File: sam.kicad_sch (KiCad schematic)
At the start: 29 parts, among them IC2 74ACT244N, IC3 74ACT244N, IC4 74ACT02, IC5 74ACT138, IC6 74ACT138N, J1 JTAG, U3 XC95144XL-TQ100, U4 AS6C1008-55TIN, U5 AS6C1008-TIN, X1 14.31818MHz

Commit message: Progress routing
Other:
- moved on the sheet: C5, C6, U5

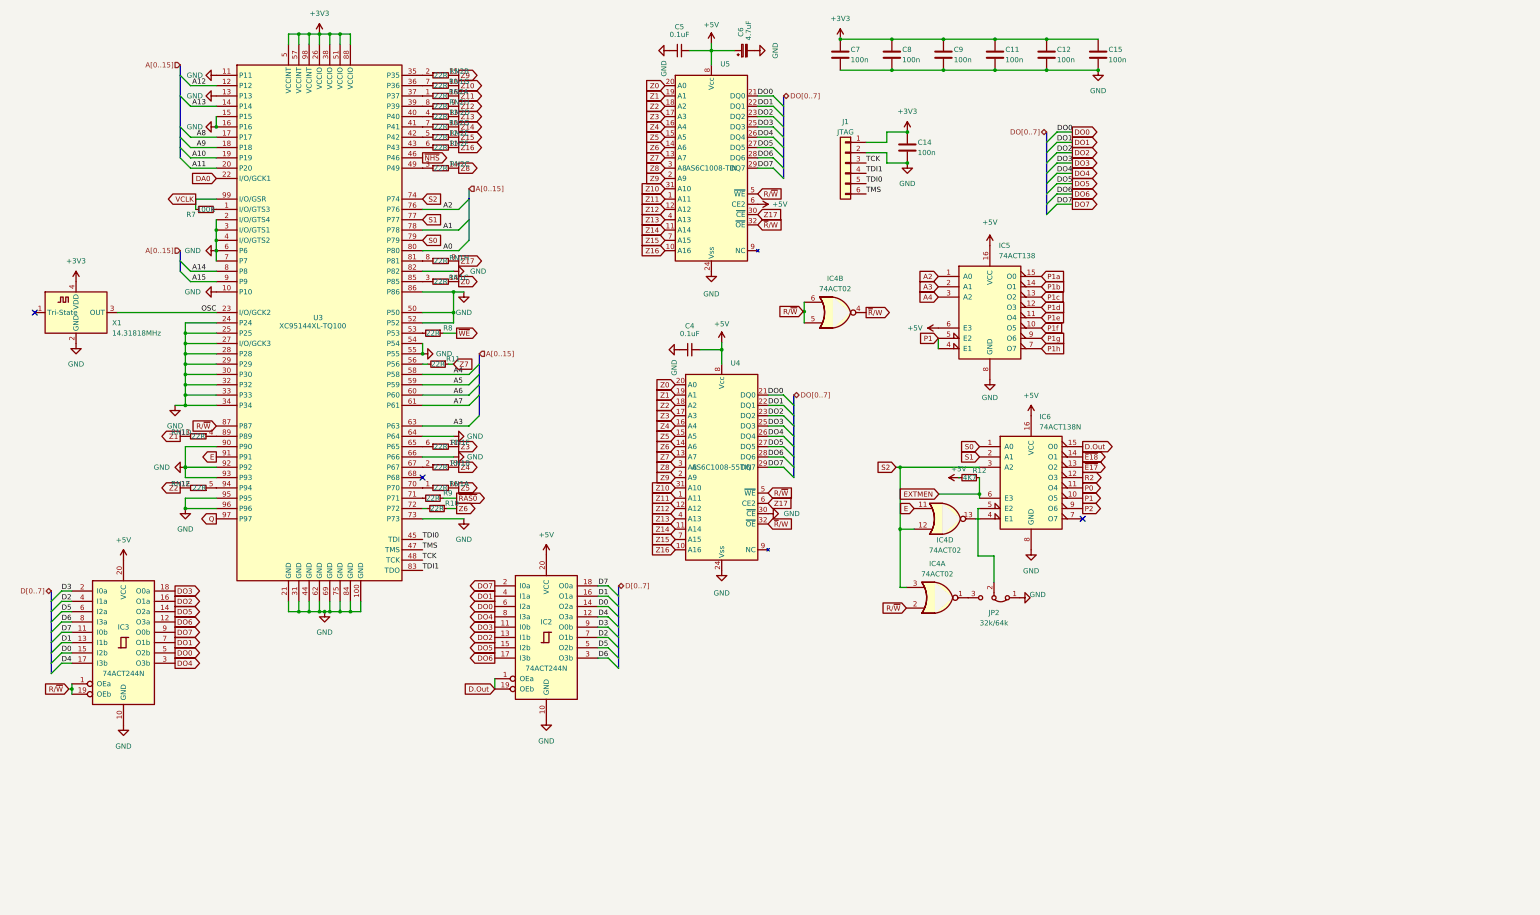
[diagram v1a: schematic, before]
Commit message: rework sram
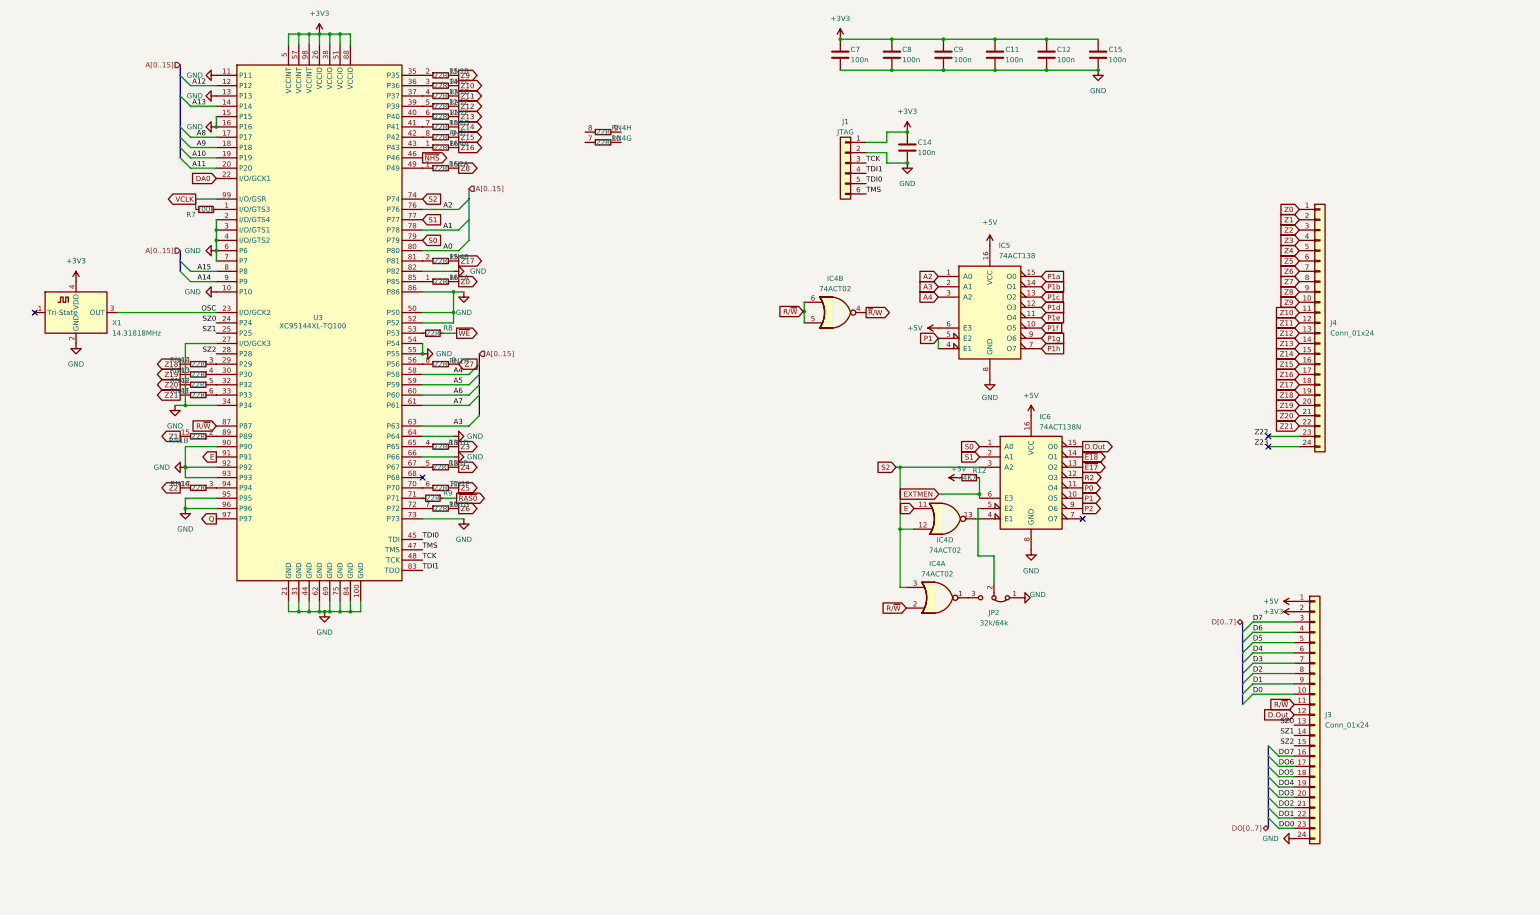
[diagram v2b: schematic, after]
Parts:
- removed C4, C5: 0.1uF, Capacitor_SMD:C_0805_2012Metric_Pad1.18x1.45mm_HandSolder, symbol Device:C_Small
- removed C6: 4.7uF, Capacitor_Tantalum_SMD:CP_EIA-3216-18_Kemet-A_Pad1.58x1.35mm_HandSolder, symbol Device:C_Polarized_Small
- removed IC2, IC3: 74ACT244N, Package_SO:SOIC-20W_7.5x12.8mm_P1.27mm, symbol 74xx:74LS244
- removed R10, R11: 22R, Resistor_SMD:R_0805_2012Metric_Pad1.20x1.40mm_HandSolder, symbol Device:R_Small
- removed U4: AS6C1008-55TIN, Package_SO:TSOP-I-32_18.4x8mm_P0.5mm, symbol Motorola PIA:AS6C1008
- removed U5: AS6C1008-TIN, Package_SO:TSOP-I-32_18.4x8mm_P0.5mm, symbol Motorola PIA:AS6C1008
- added J3, J4: Conn_01x24, Connector_PinSocket_1.27mm:PinSocket_1x24_P1.27mm_Vertical, symbol Connector_Generic:Conn_01x24
- added RN4: 22R, Package_SO:SOIC-16_3.9x9.9mm_P1.27mm, symbol Motorola PIA:R_Pack_Split
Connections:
- net +3V3: now also J3.2 (Pin_2)
- net +5V: now also J3.1 (Pin_1)
- net A14: now also U3.9 (P9); no longer U3.8 (P8)
- net A15: now also U3.8 (P8); no longer U3.9 (P9)
- net D.Out: now also J3.12 (Pin_12)
- net D0: now also J3.10 (Pin_10)
- net D1: now also J3.9 (Pin_9)
- net D2: now also J3.8 (Pin_8)
- net D3: now also J3.7 (Pin_7)
- net D4: now also J3.6 (Pin_6)
- net D5: now also J3.5 (Pin_5)
- net D6: now also J3.4 (Pin_4)
- net D7: now also J3.3 (Pin_3)
- net DO0: now also J3.23 (Pin_23)
- net DO1: now also J3.22 (Pin_22)
- net DO2: now also J3.21 (Pin_21)
- net DO3: now also J3.20 (Pin_20)
- net DO4: now also J3.19 (Pin_19)
- net DO5: now also J3.18 (Pin_18)
- net DO6: now also J3.17 (Pin_17)
- net DO7: now also J3.16 (Pin_16)
- net GND: now also J3.24 (Pin_24); no longer U3.24 (P24), U3.25 (P25), U3.28 (P28), U3.29 (P29), U3.30 (P30), U3.32 (P32), U3.33 (P33)
- net R/~{W}: now also J3.11 (Pin_11)
- net Z0: now also RN1.16, J4.1 (Pin_1); no longer RN1.14
- net Z1: now also RN1.15, J4.2 (Pin_2); no longer RN1.13
- net Z10: now also RN2.14, J4.11 (Pin_11); no longer RN1.10
- net Z11: now also RN2.13, J4.12 (Pin_12); no longer RN2.16
- net Z12: now also RN2.12, J4.13 (Pin_13); no longer RN2.9
- net Z13: now also RN2.11, J4.14 (Pin_14); no longer RN2.13
- net Z14: now also J4.15 (Pin_15)
- net Z15: now also RN2.9, J4.16 (Pin_16); no longer RN2.12
- net Z16: now also J4.17 (Pin_17), RN4.16; no longer RN2.11
- net Z17: now also J4.18 (Pin_18), RN4.15; no longer RN1.9
- net Z2: now also RN1.14, J4.3 (Pin_3); no longer RN1.12
- net Z3: now also RN1.13, J4.4 (Pin_4); no longer RN1.11
- net Z4: now also RN1.12, J4.5 (Pin_5); no longer RN1.15
- net Z5: now also RN1.11, J4.6 (Pin_6); no longer RN1.16
- net Z6: now also RN1.10, J4.7 (Pin_7)
- net Z7: now also RN1.9, J4.8 (Pin_8)
- net Z8: now also RN2.16, J4.9 (Pin_9); no longer RN2.14
- net Z9: now also J4.10 (Pin_10)
- net at RN1.6: now also U3.70 (P70); no longer U3.65 (P65)
- net at RN2.6: now also U3.40 (P40); no longer U3.43 (P43)
- net at RN2.4: now also U3.37 (P37); no longer U3.40 (P40)
- net at RN2.3: now also U3.36 (P36); no longer U3.49 (P49)
- net at RN1.8: now also U3.56 (P56); no longer U3.81 (P81)
- net at RN1.4: now also U3.65 (P65); no longer U3.89 (P89)
- net at RN1.7: now also U3.72 (P72); no longer U3.36 (P36)
- net at RN2.1: now also U3.49 (P49); no longer U3.37 (P37)
- net at RN1.2: now also U3.89 (P89); no longer U3.67 (P67)
- net at RN2.8: now also U3.42 (P42); no longer U3.39 (P39)
- net at RN1.1: now also U3.85 (P85); no longer U3.70 (P70)
- net at RN1.3: now also U3.94 (P94); no longer U3.85 (P85)
- net at RN2.5: now also U3.39 (P39); no longer U3.42 (P42)
- net at RN1.5: now also U3.67 (P67); no longer U3.94 (P94)
- new net: RN4.4, U3.30 (P30)
- new net: RN4.3, U3.29 (P29)
- new net: RN4.2, U3.81 (P81)
- new net: RN4.1, U3.43 (P43)
- new net: RN4.6, U3.33 (P33)
- new net: RN4.5, U3.32 (P32)
- new net SZ0: J3.13 (Pin_13), U3.24 (P24)
- new net SZ1: J3.14 (Pin_14), U3.25 (P25)
- new net SZ2: J3.15 (Pin_15), U3.28 (P28)
- new net Z18: J4.19 (Pin_19), RN4.14
- new net Z19: J4.20 (Pin_20), RN4.13
- new net Z20: J4.21 (Pin_21), RN4.12
- new net Z21: J4.22 (Pin_22), RN4.11
- new net Z22: J4.23 (Pin_23)
- new net Z23: J4.24 (Pin_24)
- no-connect marks 3 -> 5
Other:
- moved on the sheet: RN1A, RN1B, RN1C, RN1D, RN1E, RN1F, RN1G, RN1H, RN2A, RN2C, RN2D, RN2E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

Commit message: progress routing
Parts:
- added unit 5 of IC4
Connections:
- net +5V: now also IC4.14 (VCC)
- net GND: now also IC4.7 (GND)
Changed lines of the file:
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@@
+	)
+	(symbol
+		(lib_id "74xx:74LS02")
+		(at 377.19 214.63 0)
+		(unit 5)
+		(exclude_from_sim no)
+		(in_bom yes)
+		(on_board yes)
+		(dnp no)
+		(property "Reference" "IC4"
+			(at 377.19 219.837 0)
+			(effects
+				(font
+					(size 1.27 1.27)
+				)
+			)
+		)
+		(property "Value" "74ACT02"
+			(at 377.19 222.377 0)
+			(effects
+				(font
+					(size 1.27 1.27)
+				)
+			)
+		)
+		(property "Footprint" "Package_SO:SOIC-14_3.9x8.7mm_P1.27mm"
+			(at 377.19 214.63 0)
+			(effects
+				(font
+					(size 1.27 1.27)
+				)
+				(hide yes)
+			)
+		)
+		(property "Datasheet" "http://www.ti.com/lit/gpn/sn74ls02"
+			(at 377.19 214.63 0)
+			(effects
+				(font
+					(size 1.27 1.27)
+				)
+				(hide yes)
+			)
+		)
+		(property "Description" ""
+			(at 377.19 214.63 0)
+			(effects
+				(font
+					(size 1.27 1.27)
+				)
+				(hide yes)
+			)
+		)
+		(property "DigiKey" "MC74ACT02DR2GOSCT-ND"
+			(at 377.19 214.63 0)
+			(effects
+				(font
+					(size 1.27 1.27)
+				)
+				(hide yes)
+			)
+		)
+		(property "SA2120" "Sheet 1 (spare)"
+			(at 377.19 214.63 0)
+			(effects
+				(font
+					(size 1.27 1.27)
+				)
+				(hide yes)
+			)
+		)
+		(pin "1"
+		)
+		(pin "2"
+		)
+		(pin "3"
+		)
+		(pin "4"
+		)
+		(pin "5"
+		)
+		(pin "6"
+		)
+		(pin "10"
+		)
+		(pin "8"
+		)
+		(pin "9"
+		)
+		(pin "11"
+		)
+		(pin "12"
+		)
+		(pin "13"
+		)
+		(pin "14"
+		)
+		(pin "7"
+		)
+		(instances
+			(project "DragonRevX4Plus"
+				(path "/280624a6-9139-42c2-8c41-e9b53b8715d2/c4b589a9-2d20-48b3-b81d-9e9e3aed36b4"
+					(reference "IC4")
+					(unit 5)
+				)
+			)
+		)
 	)
 	(symbol
@@
 	)
 	(symbol
+		(lib_id "power:+5V")
+		(at 377.19 201.93 0)
+		(unit 1)
+		(exclude_from_sim no)
+		(in_bom yes)
+		(on_board yes)
+		(dnp no)
+		(fields_autoplaced yes)
+		(property "Reference" "#PWR024"
+			(at 377.19 205.74 0)
+			(effects
+				(font
+					(size 1.27 1.27)
+				)
+				(hide yes)
+			)
+		)
+		(property "Value" "+5V"
+			(at 377.19 196.977 0)
+			(effects
+				(font
+					(size 1.27 1.27)
+				)
+			)
+		)
+		(property "Footprint" ""
+			(at 377.19 201.93 0)
+			(effects
+				(font
+					(size 1.27 1.27)
+				)
+				(hide yes)
+			)
+		)
+		(property "Datasheet" ""
+			(at 377.19 201.93 0)
+			(effects
+				(font
+					(size 1.27 1.27)
+				)
+				(hide yes)
+			)
+		)
+		(property "Description" ""
+			(at 377.19 201.93 0)
+			(effects
+				(font
+					(size 1.27 1.27)
+				)
+				(hide yes)
+			)
+		)
+		(pin "1"
+		)
+		(instances
+			(project "DragonRevX4Plus"
+				(path "/280624a6-9139-42c2-8c41-e9b53b8715d2/c4b589a9-2d20-48b3-b81d-9e9e3aed36b4"
+					(reference "#PWR024")
+					(unit 1)
+				)
+			)
+		)
+	)
+	(symbol
 		(lib_id "power:GND")
 		(at 228.6 50.8 0)
@@
 					(unit 1)
 				)
+			)
+		)
+	)
+	(symbol
+		(lib_id "power:GND")
+		(at 377.19 227.33 0)
+		(unit 1)
+		(exclude_from_sim no)
+		(in_bom yes)
+		(on_board yes)
+		(dnp no)
+		(fields_autoplaced yes)
+		(property "Reference" "#PWR025"
+			(at 377.19 233.68 0)
+			(effects
+				(font
+					(size 1.27 1.27)
+				)
+				(hide yes)
+			)
+		)
+		(property "Value" "GND"
+			(at 377.19 232.537 0)
+			(effects
+				(font
+					(size 1.27 1.27)
+				)
+			)
+		)
+		(property "Footprint" ""
+			(at 377.19 227.33 0)
+			(effects
+				(font
+					(size 1.27 1.27)
+				)
+				(hide yes)
+			)
+		)
+		(property "Datasheet" ""
+			(at 377.19 227.33 0)
+			(effects
+				(font
+					(size 1.27 1.27)
+				)
+				(hide yes)
+			)
+		)
+		(property "Description" ""
+			(at 377.19 227.33 0)
+			(effects
+				(font
+					(size 1.27 1.27)
+				)
+				(hide yes)
+			)
+		)
+		(pin "1"
+		)
+		(instances
+			(project "DragonRevX4Plus"
+				(path "/280624a6-9139-42c2-8c41-e9b53b8715d2/c4b589a9-2d20-48b3-b81d-9e9e3aed36b4"
+					(reference "#PWR025")
+					(unit 1)
+				)

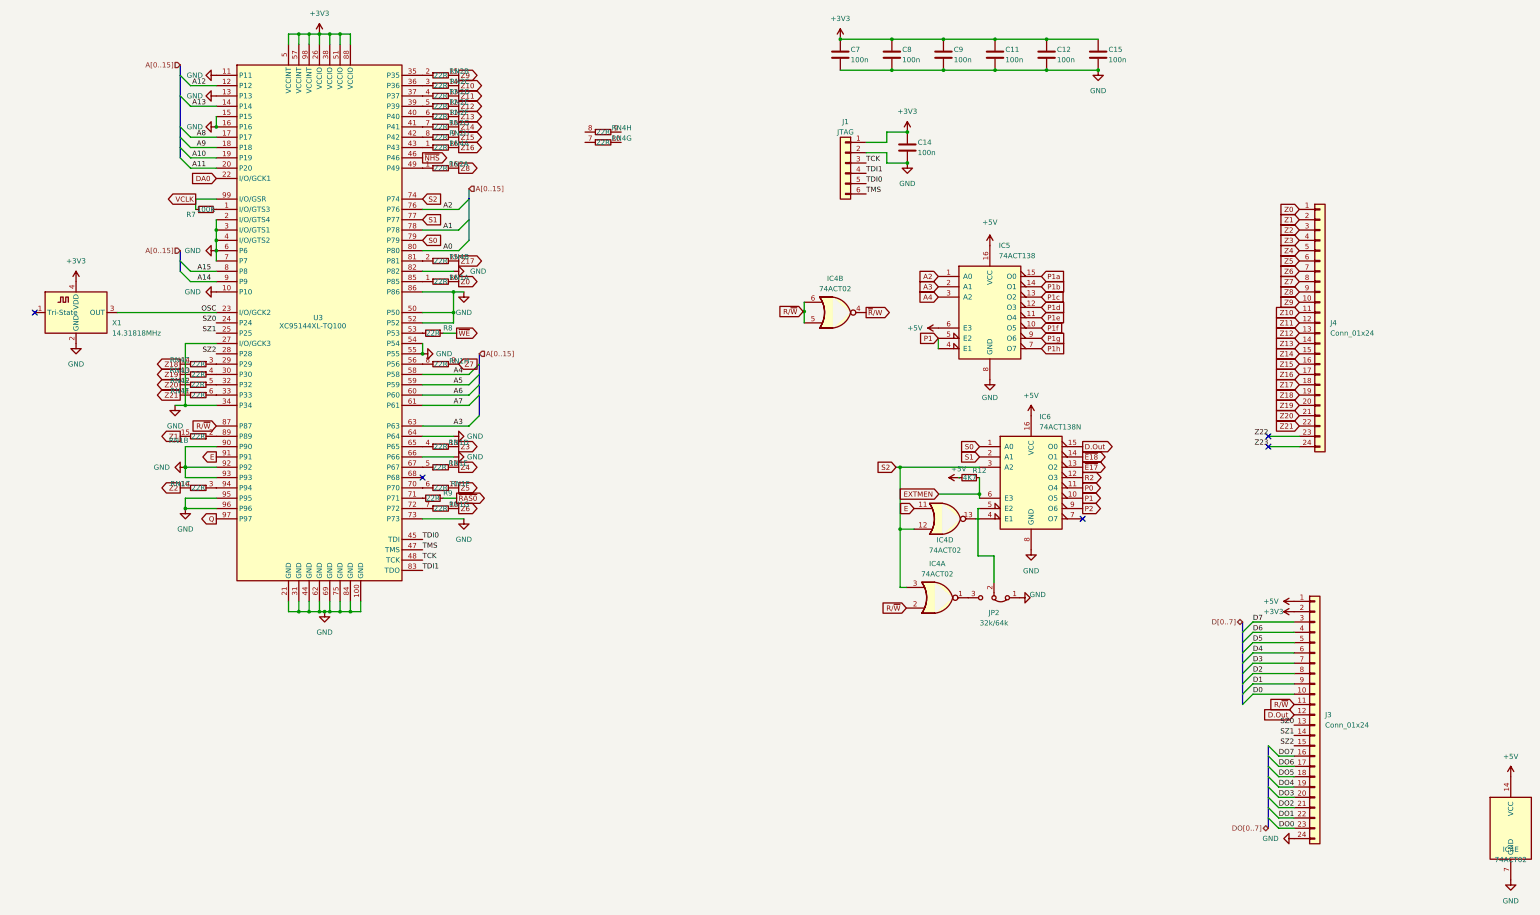
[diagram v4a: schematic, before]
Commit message: migrate to flash rom
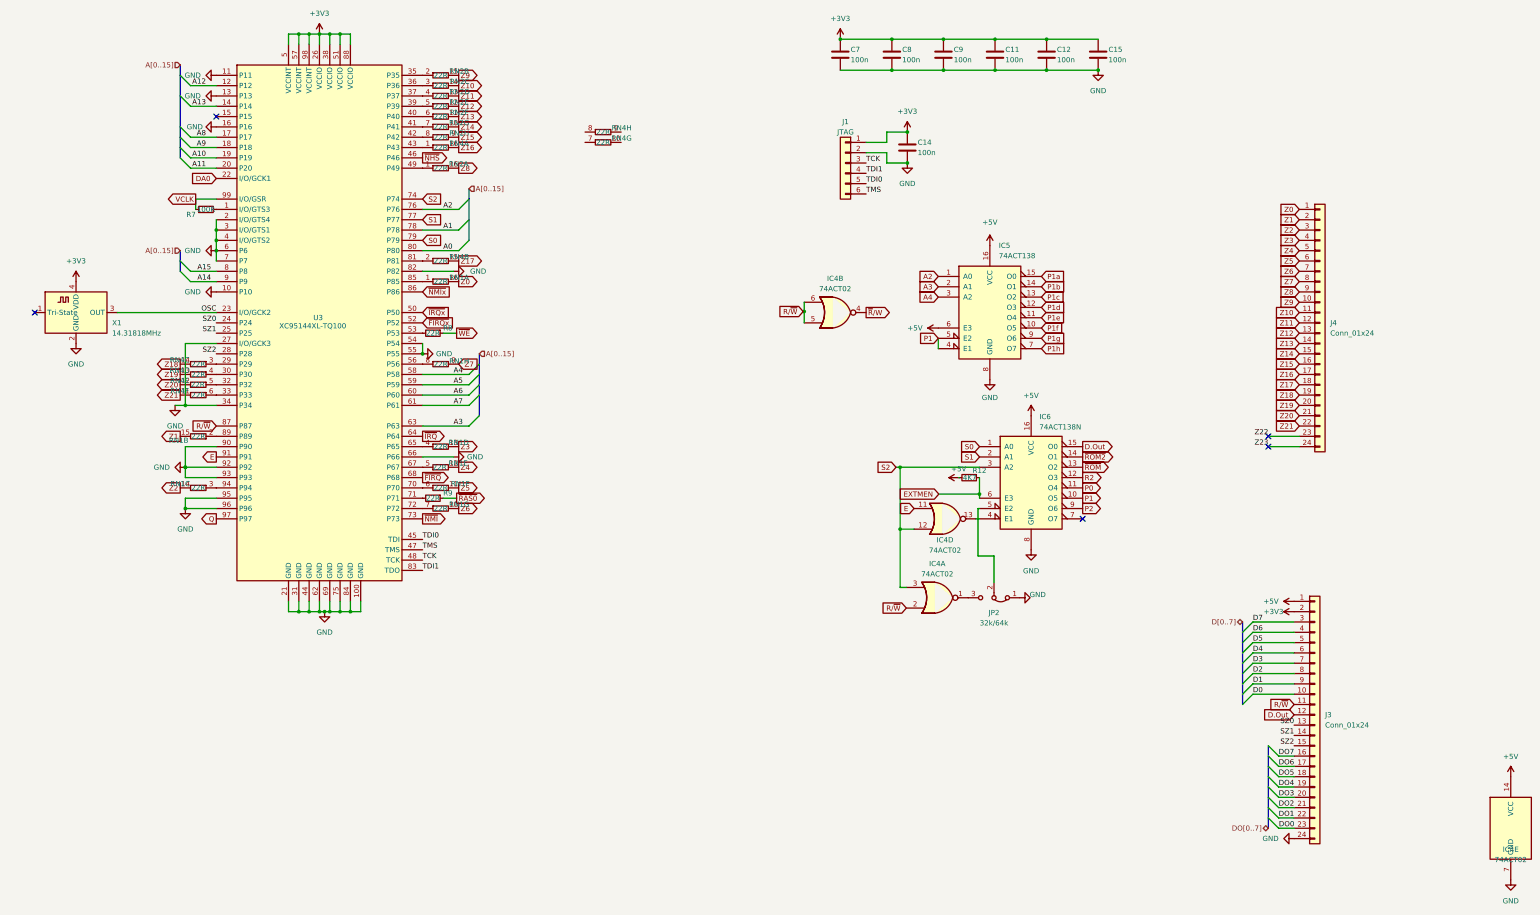
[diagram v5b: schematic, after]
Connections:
- net GND: no longer U3.15 (P15), U3.50 (P50), U3.52 (P52), U3.64 (P64), U3.73 (P73), U3.86 (P86)
- net ~{FIRQ}: now reaches U3.68 (P68)
- net ~{E17} renamed ~{ROM}
- net ~{E18} renamed ~{ROM2}
- new net ~{FIRQx}: U3.52 (P52)
- new net ~{IRQx}: U3.50 (P50)
- new net ~{IRQ}: U3.64 (P64)
- new net ~{NMIx}: U3.86 (P86)
- new net ~{NMI}: U3.73 (P73)

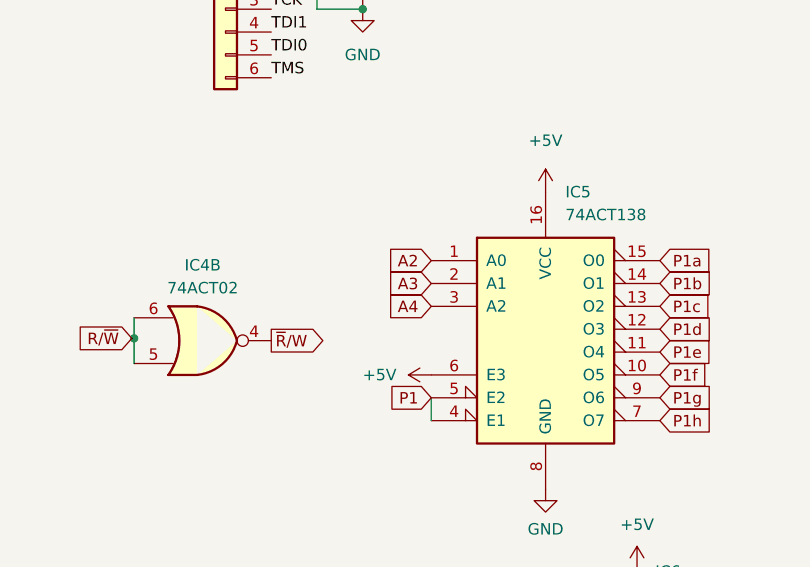
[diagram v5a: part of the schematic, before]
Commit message: complete routing
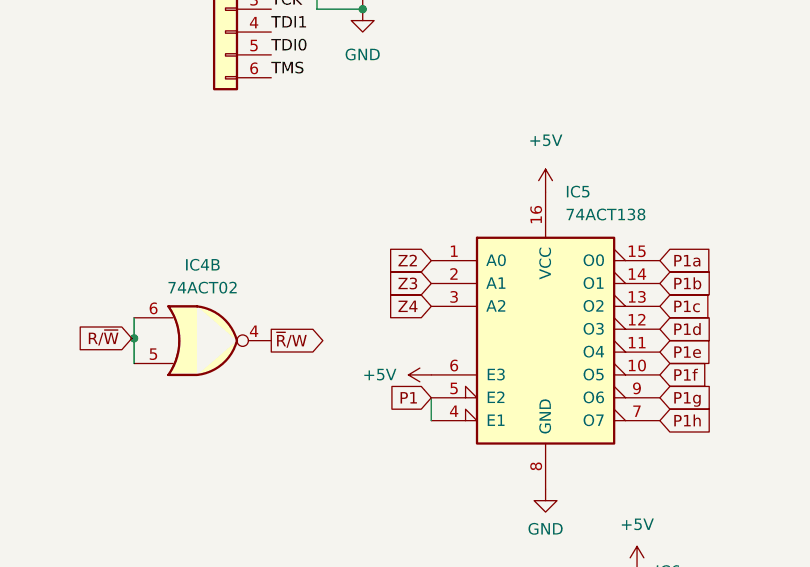
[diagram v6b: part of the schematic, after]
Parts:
- J4: AliExpress (none) -> https://www.aliexpress.com/item/1005001412414804.html?spm=a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
- RN1: footprint Package_SO:SOIC-16_3.9x9.9mm_P1.27mm -> Package_SO:SOIC-16W_5.3x10.2mm_P1.27mm; DigiKey (none) -> 4816P-T01-220LF-ND
- RN2, RN4: footprint Package_SO:SOIC-16_3.9x9.9mm_P1.27mm -> Package_SO:SOIC-16W_5.3x10.2mm_P1.27mm
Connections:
- net A2: no longer IC5.1 (A0)
- net A3: no longer IC5.2 (A1)
- net A4: no longer IC5.3 (A2)
- net Z2: now also IC5.1 (A0)
- net Z3: now also IC5.2 (A1)
- net Z4: now also IC5.3 (A2)
